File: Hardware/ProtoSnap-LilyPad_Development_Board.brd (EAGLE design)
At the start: 104.1 x 72.4 mm, 158 parts, among them M1 MOTORSMD, U1 ATMEGA328, U2 MCP9700, U3 TEMT6000, U4 MCP73831, Y1 8MHz

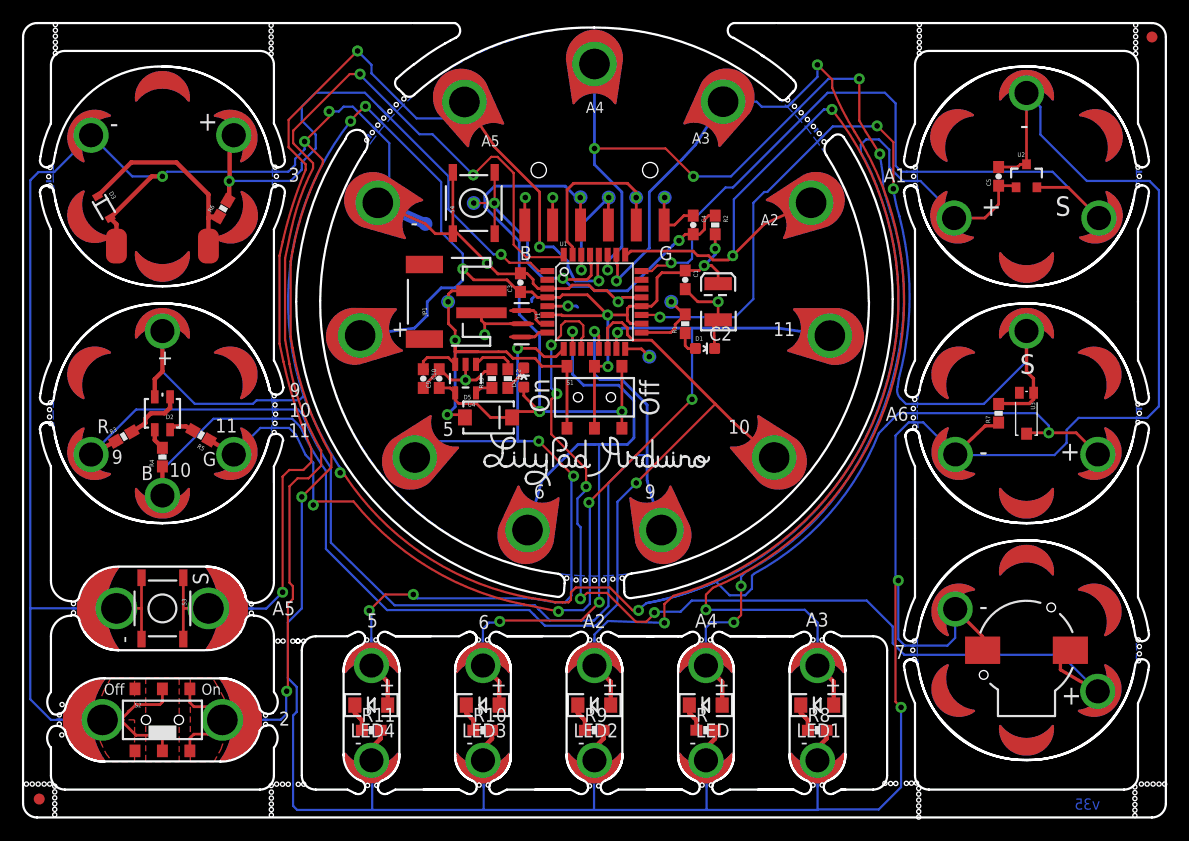
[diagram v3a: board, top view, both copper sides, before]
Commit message: Common Cathode LED, ALS-PT19 light sensor
Also added measures and "route out" text.
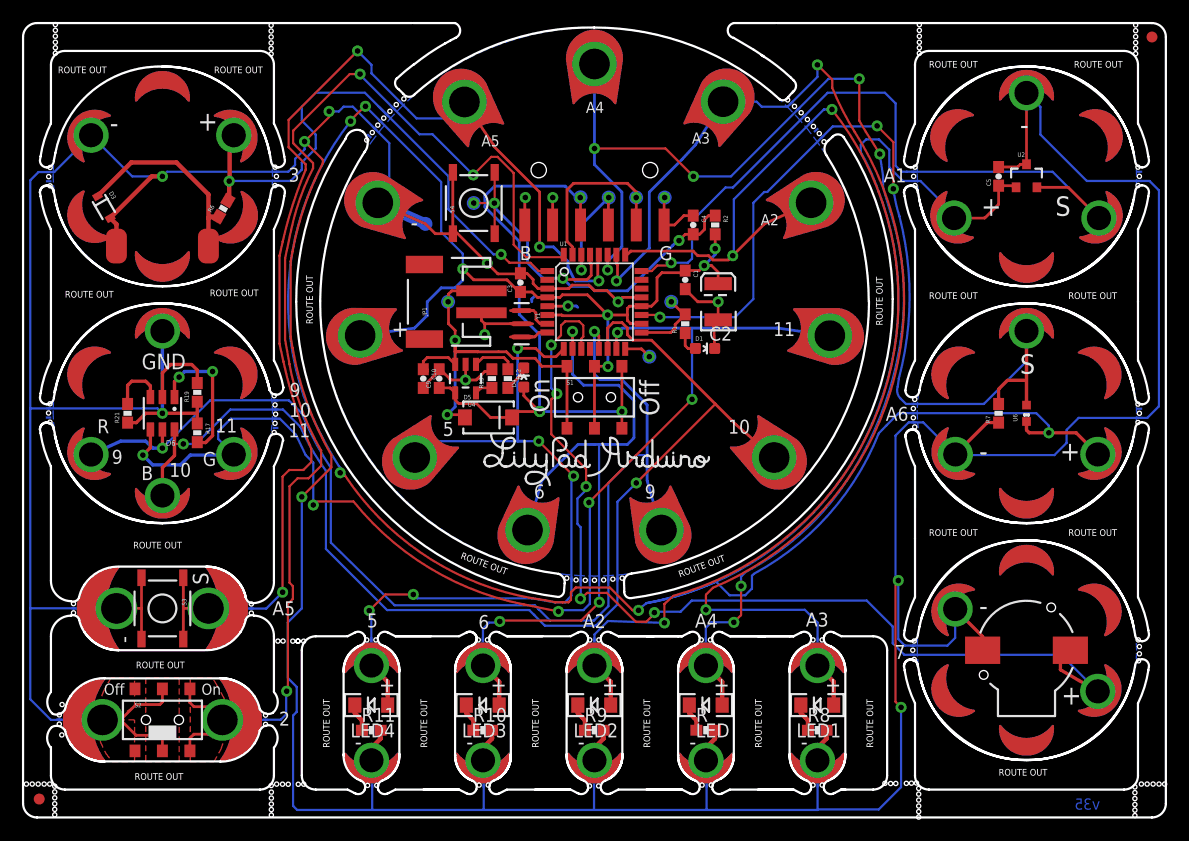
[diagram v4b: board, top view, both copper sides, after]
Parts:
- removed D2: LED-TRICOLOR, SparkFun:LED-TRICOLOR-SMD
- removed FRAME2: FRAME-LEDGER, SparkFun-Aesthetics:CREATIVE_COMMONS
- removed R3: 200, SparkFun:0603-RES
- removed R4, R5: 100, SparkFun:0603-RES
- removed U3: TEMT6000, SparkFun:TEMT6000-SEN
- added D6: LED-TRICOLOR, SparkFun-LED:PLCC-6-LED
- added FRAME1: FRAME-LEDGER, SparkFun-Aesthetics:CREATIVE_COMMONS
- added R17: 300, SparkFun-Resistors:0603-RES
- added R19, R21: 100, SparkFun-Resistors:0603-RES
- added U6: LIGHTSENSOR_ALS-PT19, SparkFun-Sensors:ALS-PT19
- U$48: value MOUSE-BITE-3(NO_PADS) -> MOUSE-BITE-2; device Testing:MOUSE-BITE-3(NO_PADS) -> Testing:MOUSE-BITE-2
- moved U$48 0.09 mm to (2.32, 36.9)
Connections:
- removed net BLU: D2.B, R4.2
- removed net GRN: D2.G, R5.2
- removed net RED: D2.R, R3.2
- new net BLUE: D6.CB, R17.2
- new net GRN1: D6.CG, R21.2
- new net RED1: D6.CR, R19.2
- net A6: now also U6.E; no longer U3.EMITTER
- net D10: now also D6.AB, U$20.P$3; no longer R4.1, U$20.P$2
- net D11: now also D6.AG, U$20.P$2; no longer R5.1, U$20.P$1
- net D9: now also D6.AR, U$20.P$4; no longer R3.1, U$20.P$3
- net GND: now also R17.1, R19.1, R21.1, U$25.1, U$48.P$1
- net VCC: now also U6.C; no longer D2.A, U$20.P$4, U$25.1, U3.COLLECTOR
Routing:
- net GND: track 474.3 -> 502.9 mm, vias 14 -> 15
- net VCC: track 304.0 -> 280.2 mm
- net D11: track 97.1 -> 110.0 mm, vias 5 -> 6
- net BLUE: track 0.00 -> 12.8 mm, vias 0 -> 2
- net RED1: track 0.00 -> 7.15 mm
- net RED: track 5.53 -> 0.00 mm
- net GRN1: track 0.00 -> 5.12 mm
- net BLU: track 2.69 -> 0.00 mm
- net GRN: track 2.58 -> 0.00 mm
- net A6: track 85.5 -> 86.6 mm
- net D10: track 106.4 -> 106.5 mm, vias 1 -> 2
- net D9: track 103.9 -> 104.0 mm, vias 1 -> 2
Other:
- board text added: "GND"
- board text added: "ROUTE OUT"

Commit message: Schematic cleanup
-Fixed 4-way junction off of MCP73831
-cleaned up nets off of snap-able leds
-added sch note and box for programming testpoints
-moved to flag label on D7
-removed value labels on pedals near motor
-corrected diode prefixes
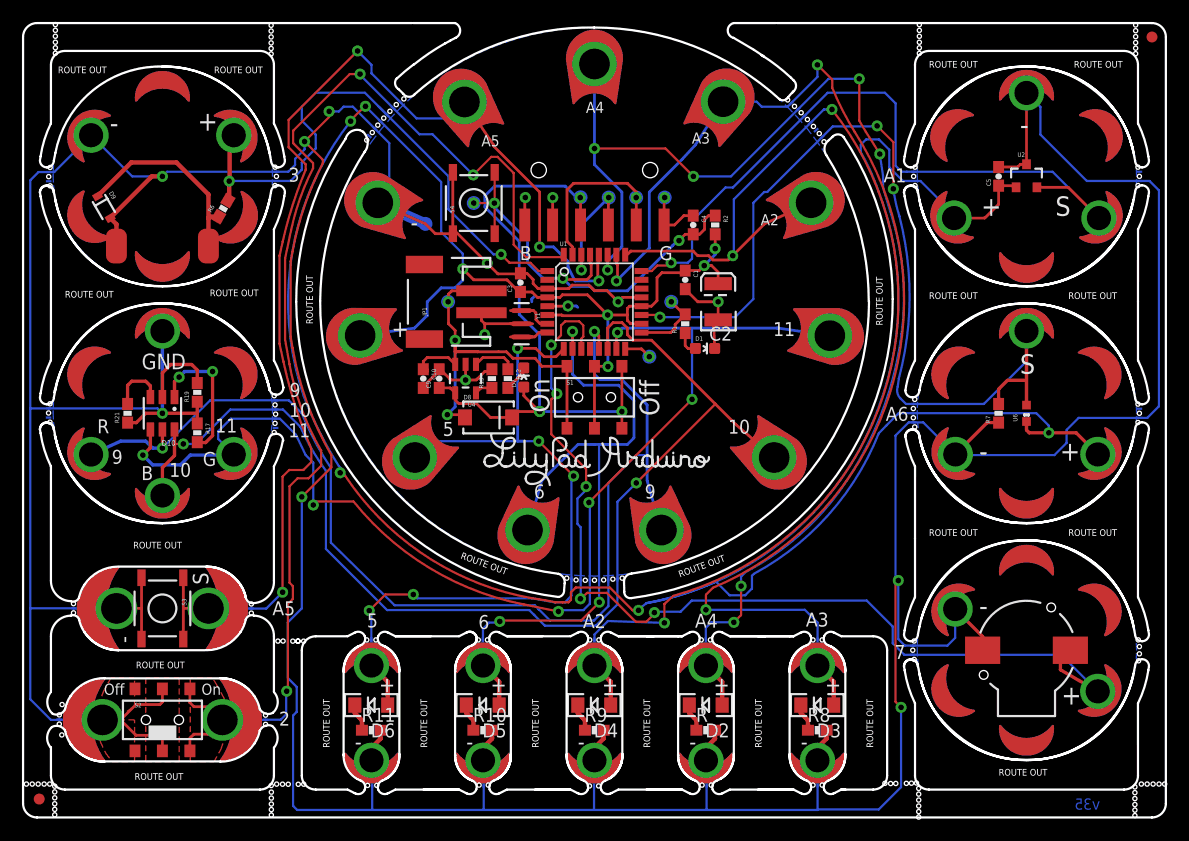
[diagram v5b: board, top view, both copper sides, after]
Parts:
- removed LED1, LED2, LED3, LED4: White, SparkFun-3-2-07:LED-1206
- added D10: LED-TRICOLOR, SparkFun-LED:PLCC-6-LED
- added D7: Yellow, Testing:0603-LED-ALT1
- added D8: B340A, SparkFun-DiscreteSemi:SMA-DIODE
- added D9: (no value), SparkFun:SOD-323
- D3: value (none) -> White; device SparkFun:SOD-323 -> SparkFun-3-2-07:LED-1206
- D4: value Yellow -> White; device Testing:0603-LED-ALT1 -> SparkFun-3-2-07:LED-1206
- D5: value B340A -> White; device SparkFun-DiscreteSemi:SMA-DIODE -> SparkFun-3-2-07:LED-1206
- D6: value LED-TRICOLOR -> White; device SparkFun-LED:PLCC-6-LED -> SparkFun-3-2-07:LED-1206
- M1: value MOTORSMD -> VIBE MOTOR
- moved D3 79.3 mm to (72.4, 10.2), turned to 180 degrees
- moved D6 32.7 mm to (31.7, 10.2)
- moved D4 30.5 mm to (52.0, 10.2), turned to 180 degrees
- moved D5 26.2 mm to (41.9, 10.2), turned to 180 degrees
- renumbered LED to D2
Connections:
- net BLUE: now also D10.CB; no longer D6.CB
- net D10: now also D10.AB; no longer D6.AB
- net D11: now also D10.AG; no longer D6.AG
- net D9: now also D10.AR; no longer D6.AR
- net FTDI_VCC: now also D7.A, D8.C; no longer D4.A, D5.C
- net GND: now also D9.2; no longer D3.2
- net GRN1: now also D10.CG; no longer D6.CG
- net N$10: now also D9.1; no longer D3.1
- net N$21: now also D3.C; no longer LED1.C
- net N$22: now also D3.A; no longer LED1.A
- net N$24: now also D4.C; no longer LED2.C
- net N$25: now also D4.A; no longer LED2.A
- net N$27: now also D5.C; no longer LED3.C
- net N$28: now also D5.A; no longer LED3.A
- net N$30: now also D6.C; no longer LED4.C
- net N$31: now also D6.A; no longer LED4.A
- net N$33: now also D7.C; no longer D4.C
- net RED1: now also D10.CR; no longer D6.CR
- net VBATT: now also D8.A; no longer D5.A

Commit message: Adding Prod IDs (not 100% done)
Also had to reroute traces off of IC
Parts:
- removed U1: ATMEGA328, SparkFun:TQFP32-08
- added U3: ATMEGA328P_TQFP, SparkFun-DigitalIC:TQFP32-08
- B1: device SparkFun:BUZZER-CCV -> SparkFun-Electromechanical:BUZZER-CCV
- C1, C10, C3, C4, C9: device SparkFun:0603-CAP -> SparkFun-Capacitors:0603-CAP
- C2: device SparkFun:EIA3528 -> SparkFun-Capacitors:EIA3528
- R, R1, R10, R11, R12, R2, R7, R8, R9: device SparkFun:0603-RES -> SparkFun-Resistors:0603-RES
- R13: value 1k -> 1K; device SparkFun:0603-RES -> SparkFun-Resistors:0603-RES
- R6: value 33 -> 33OHM; device SparkFun:0603-RES -> SparkFun-Resistors:0603
- U2: device SparkFun:SOT23-3 -> SparkFun-Sensors:SOT23-3
- U4: device SparkFun:SOT23-5 -> SparkFun-PowerIC:SOT23-5
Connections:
- net A1: now also U3.24; no longer U1.24
- net A2: now also U3.25; no longer U1.25
- net A3: now also U3.26; no longer U1.26
- net A4: now also U3.27; no longer U1.27
- net A5: now also U3.28; no longer U1.28
- net A6: now also U3.19; no longer U1.19
- net D10: now also U3.14; no longer U1.14
- net D11: now also U3.15; no longer U1.15
- net D12: now also U3.16; no longer U1.16
- net D13: now also U3.17; no longer U1.17
- net D2: now also U3.32; no longer U1.32
- net D3: now also U3.1; no longer U1.1
- net D5: now also U3.9; no longer U1.9
- net D6: now also U3.10; no longer U1.10
- net D7: now also U3.11; no longer U1.11
- net D9: now also U3.13; no longer U1.13
- net GND: now also U3.21, U3.3, U3.5; no longer U1.21, U1.3, U1.5
- net N$1: now also U3.7; no longer U1.7
- net N$3: now also U3.8; no longer U1.8
- net RST: now also U3.29; no longer U1.29
- net RXI: now also U3.30; no longer U1.30
- net TXO: now also U3.31; no longer U1.31
- net VCC: now also U3.18, U3.20, U3.4, U3.6; no longer U1.18, U1.20, U1.4, U1.6
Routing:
- net VCC: track 280.2 -> 281.2 mm
- net GND: track 502.9 -> 502.3 mm, vias 15 -> 16
- net A5: track 109.3 -> 108.8 mm
- net FTDI_VCC: vias 4 -> 3

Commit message: More schematic cleanup
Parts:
- M1: value VIBE MOTOR -> VIBE
- S2: value AYZ0202 -> (none)
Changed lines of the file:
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@@
 <layer number="49" name="Reference" color="11" fill="1" visible="no" active="yes"/>
 <layer number="50" name="dxf" color="7" fill="1" visible="no" active="yes"/>
-<layer number="51" name="tDocu" color="6" fill="1" visible="no" active="yes"/>
+<layer number="51" name="tDocu" color="6" fill="1" visible="yes" active="yes"/>
 <layer number="52" name="bDocu" color="7" fill="1" visible="no" active="yes"/>
 <layer number="53" name="tGND_GNDA" color="7" fill="9" visible="no" active="no"/>
@@
 <element name="VIBE-" library="LilyPad-Wearables" package="PETAL-SMALL-2SIDE" value="SEWTAP6" x="6.2" y="62.17" rot="R240"/>
 <element name="VIBE+" library="LilyPad-Wearables" package="PETAL-SMALL-2SIDE" value="SEWTAP6" x="19.1987" y="62.1699" rot="R120"/>
-<element name="M1" library="Testing" package="VIBE-MOTOR-10MM-SMD" value="VIBE MOTOR" x="12.7" y="59.309"/>
+<element name="M1" library="Testing" package="VIBE-MOTOR-10MM-SMD" value="VIBE" x="12.7" y="59.309"/>
 <element name="D9" library="SparkFun" package="SOD-323" value="" x="7.366" y="55.626" rot="R300"/>
 <element name="VIBE4" library="LilyPad-Wearables" package="PETAL-NOHOLE-2SIDE" value="SEWTAP-NOHOLE2" x="12.7" y="65.92" rot="R180"/>
@@
 <element name="LIGHTS" library="LilyPad-Wearables" package="PETAL-SMALL-2SIDE" value="SEWTAP6" x="91.44" y="44.33" rot="R180"/>
 <element name="U$31" library="LilyPad-Wearables" package="LOGO-LILYPAD" value="LOGO-LPLP" x="91.44" y="36.83" rot="MR0"/>
-<element name="S2" library="SparkFun" package="AYZ0202" value="AYZ0202" x="12.7" y="8.89"/>
+<element name="S2" library="SparkFun" package="AYZ0202" value="" x="12.7" y="8.89"/>
 <element name="SLIDEOFF" library="LilyPad-Wearables" package="PETAL-MEDIUM-2SIDE" value="SEWTAP8" x="7.493" y="8.89" rot="R270"/>
 <element name="SLIDEON" library="LilyPad-Wearables" package="PETAL-MEDIUM-2SIDE" value="SEWTAP8" x="17.907" y="8.89" rot="R90"/>
@@
 <via x="35.56" y="20.32" extent="1-16" drill="0.508"/>
 <wire x1="46.7147" y1="42.7441" x2="45.07" y2="42.7441" width="0.254" layer="1"/>
-<wire x1="48.5586" y1="41.9862" x2="48.0822" y2="41.9862" width="0" layer="19" extent="1-16"/>
 <wire x1="48.0822" y1="41.9862" x2="47.4726" y2="41.9862" width="0.254" layer="1"/>
 <wire x1="47.4726" y1="41.9862" x2="46.7147" y2="42.7441" width="0.254" layer="1"/>

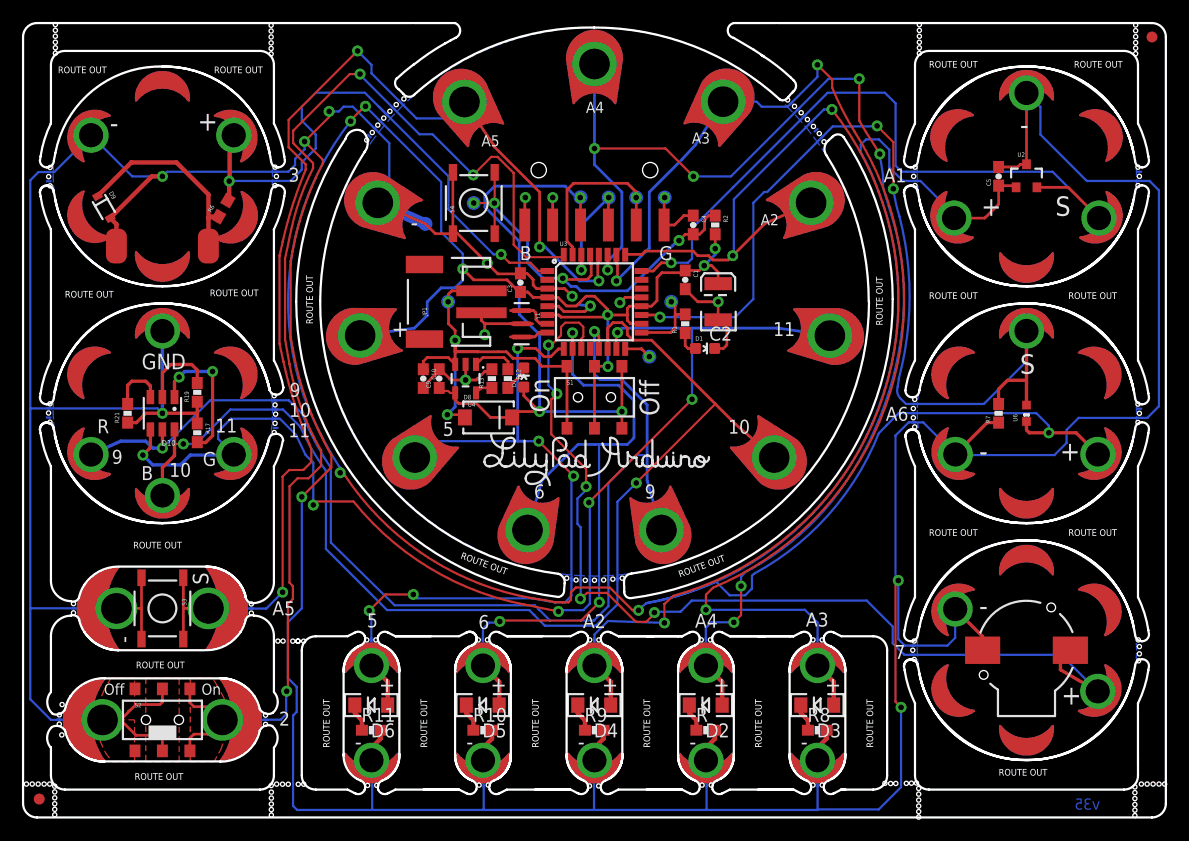
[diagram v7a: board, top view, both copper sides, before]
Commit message: fixing some acid traps and scooting some component
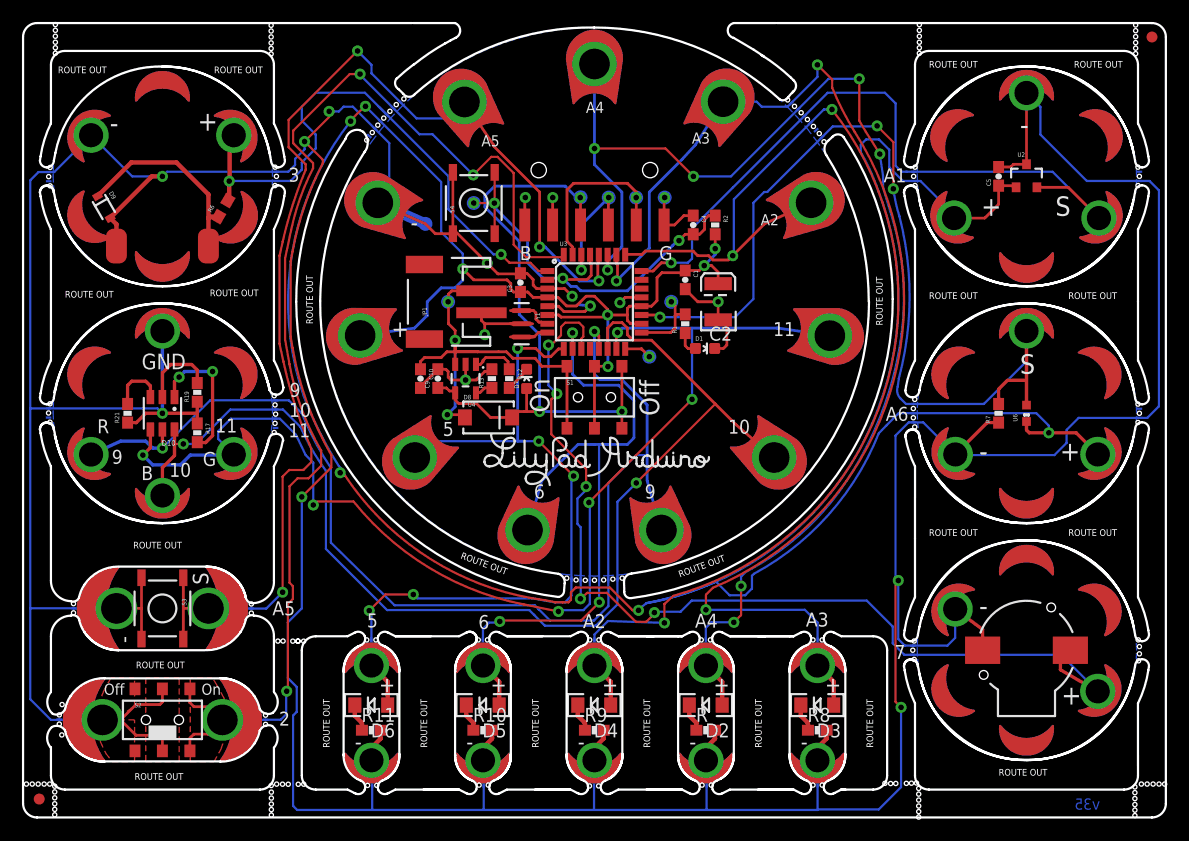
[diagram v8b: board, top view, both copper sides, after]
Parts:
- Y1: value 8MHz -> 8MHZ
- moved D7 0.28 mm to (45.9, 40.0)
- moved C10 0.25 mm to (36.2, 40.0)
- moved C9 0.13 mm to (37.8, 40.0)
- moved R12 0.13 mm to (44.3, 40.0)
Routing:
- net GND: track 502.3 -> 503.1 mm
- net FTDI_VCC: track 60.6 -> 60.0 mm
- net VBATT: track 42.9 -> 42.4 mm
